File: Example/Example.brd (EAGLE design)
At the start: 86 x 54 mm, 14 parts, among them IC1 LM555D, J1 UX60-MB-5S8, Q1 SSM3J356R, Q2 BSS806N, SW1 MFS101D-6-Z

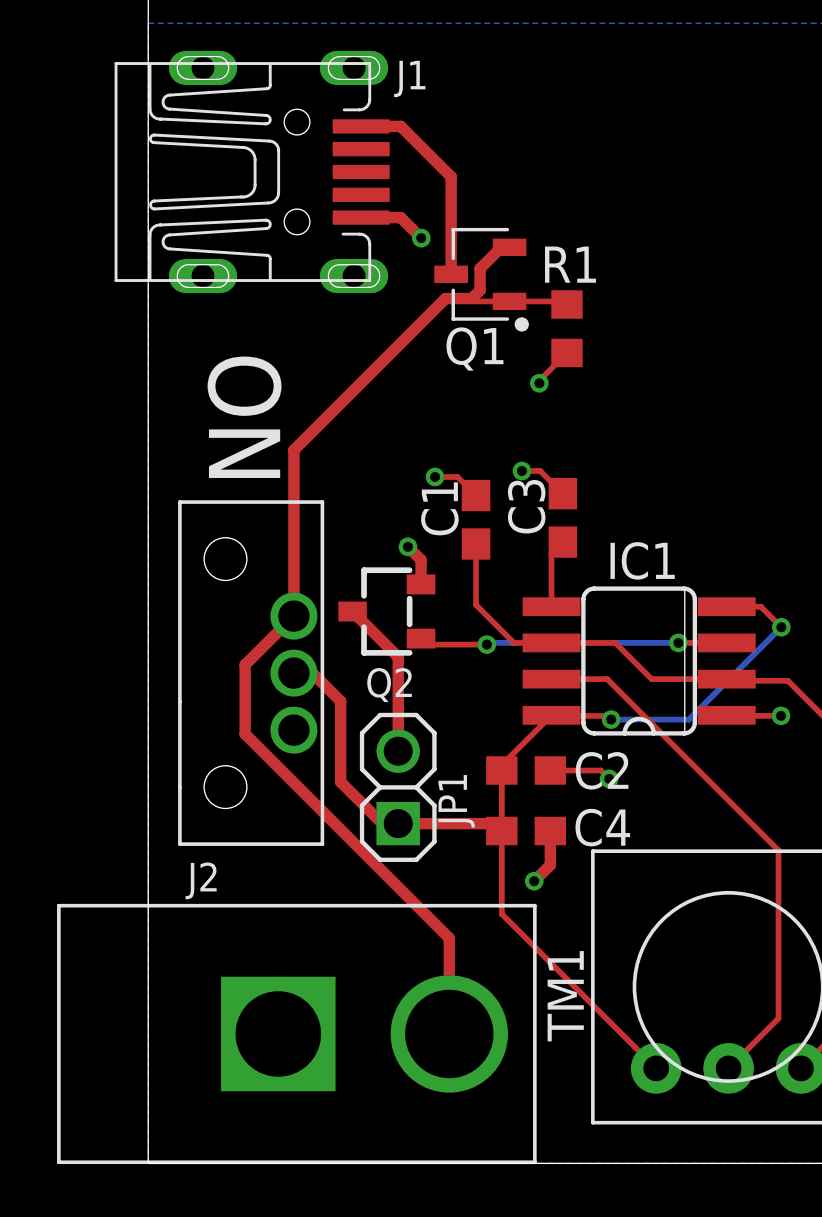
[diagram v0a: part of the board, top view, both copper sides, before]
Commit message: Fixed broken circuit and made new render
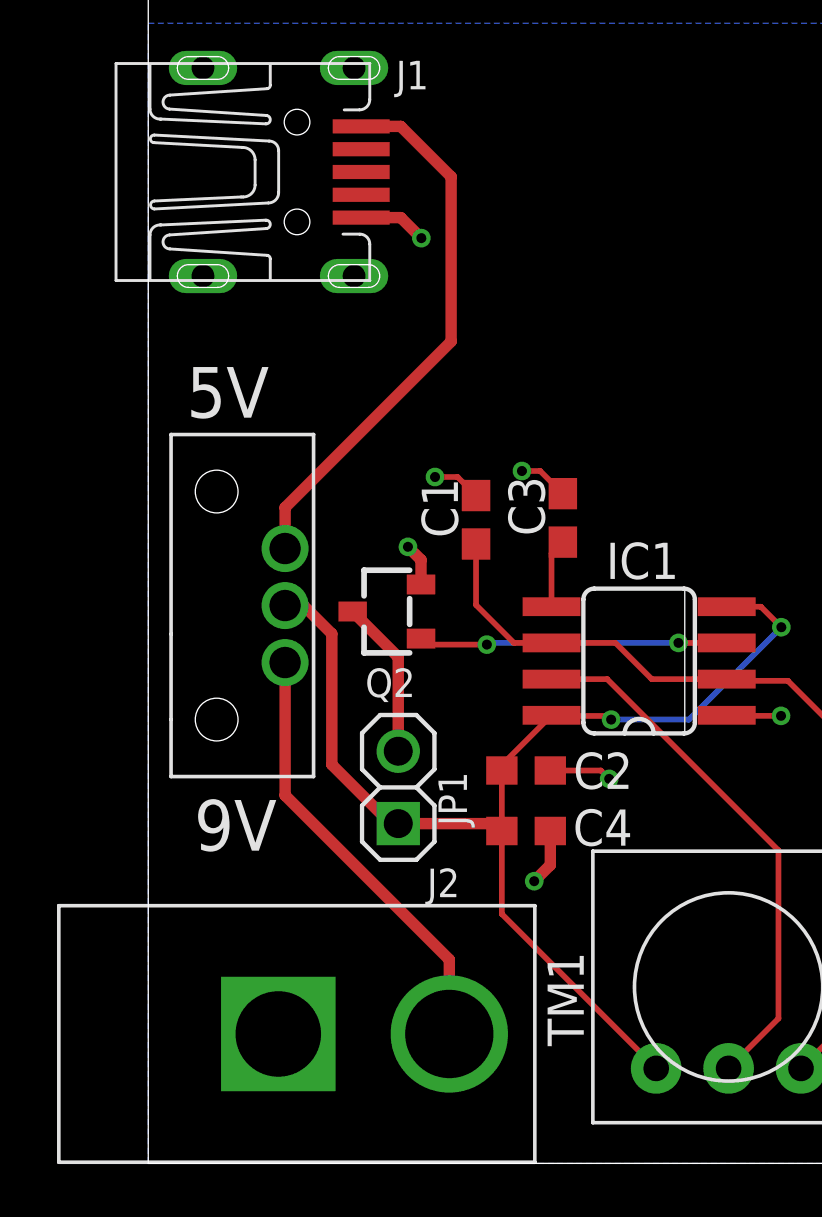
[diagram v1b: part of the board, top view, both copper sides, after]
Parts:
- removed Q1: SSM3J356R, Example:SOT95P240X80-3N
- removed R1: 10K, rcl:R0603
- moved SW1 2.39 mm to (4.80, 19.6)
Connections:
- net GND: no longer R1.1
- net N$4: now also SW1.3; no longer Q1.3
- net N$6: now also SW1.1; no longer Q1.1, Q1.2, R1.2, SW1.3
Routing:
- net N$6: track 38.5 -> 15.4 mm
- net N$4: track 7.31 -> 19.3 mm
- net +9V: track 38.3 -> 40.6 mm
- net GND: track 14.9 -> 13.5 mm, vias 8 -> 7
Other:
- board text added: "5V"
- board text added: "9V"
- board text removed: "ON"
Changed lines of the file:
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@@
 <?xml version="1.0" encoding="utf-8"?>
 <!DOCTYPE eagle SYSTEM "eagle.dtd">
-<eagle version="9.6.2">
+<eagle version="9.5.2">
 <drawing>
 <settings>
-<setting alwaysvectorfont="no"/>
+<setting alwaysvectorfont="yes"/>
 <setting verticaltext="up"/>
 </settings>
-<grid distance="50" unitdist="mil" unit="mil" style="lines" multiple="1" display="no" altdistance="5" altunitdist="mil" altunit="mil"/>
+<grid distance="0.01" unitdist="mm" unit="mm" style="lines" multiple="1" display="no" altdistance="5" altunitdist="mil" altunit="mil"/>
 <layers>
 <layer number="1" name="Top" color="4" fill="1" visible="yes" active="yes"/>
@@
 </layers>
 <board>
-<fusionsync huburn="a.cGVyc29uYWw6dWUyY2EyMWFk" projecturn="a.cGVyc29uYWw6dWUyY2EyMWFkIzIwMjAxMTI1MzU2ODEzNTgx" f3durn="urn:adsk.wipprod:dm.lineage:dyqZrbbKTy2XcHXfwjEQZg" pcbguid="" lastpulledtime="" lastsyncedchangeguid="" latestrevisionid="17bb6422-26a5-4a22-a8fc-66dc1e53293f" lastsyncedrevisionid="17bb6422-26a5-4a22-a8fc-66dc1e53293f" lastboardhashguid="af3778a2-1b63-800d-478d-2496b3e21cb4" lastpushedtime="2020-11-26T02:07:45Z" linktopcb3d="false"/>
 <plain>
 <wire x1="0" y1="0" x2="86" y2="0" width="0" layer="20"/>
@@
 <wire x1="86" y1="54" x2="0" y2="54" width="0" layer="20"/>
 <wire x1="0" y1="54" x2="0" y2="0" width="0" layer="20"/>
-<text x="2.13" y="28.48" size="2.5" layer="21" font="vector" rot="SR270">ON</text>
 <text x="30.58" y="2.23" size="1.778" layer="21" font="vector" rot="R90">RoboJackets PCB Contest
 555 Timer PWM Motor Driver</text>
 <dimension x1="0" y1="54" x2="0" y2="0" x3="-13.1" y3="27" textsize="1.778" layer="51" dtype="vertical"/>
 <dimension x1="0" y1="54" x2="86" y2="54" x3="43" y3="63.84" textsize="1.778" layer="51" dtype="horizontal"/>
+<text x="1.34" y="26.16" size="1.778" layer="21">5V</text>
+<text x="1.61" y="10.97" size="1.778" layer="21">9V</text>
 </plain>
 <attributes>
@@
 </element>
 <element name="TM1" library="adafruit" library_urn="urn:adsk.eagle:library:420" package="TRIM-3386" package3d_urn="urn:adsk.eagle:package:6240934/1" value="" x="20.36" y="6.19" smashed="yes">
-<attribute name="NAME" x="15.28" y="4.285" size="1.27" layer="25" font="vector" rot="R90"/>
+<attribute name="NAME" x="15.28" y="4.115" size="1.27" layer="25" font="vector" rot="R90"/>
 <attribute name="VALUE" x="26.71" y="4.285" size="1.27" layer="27" rot="R90"/>
 </element>
 <element name="J2" library="RoboJackets-Connectors" package="PJ-037A" override_package3d_urn="urn:adsk.eagle:package:25000921/2" override_package_urn="urn:adsk.eagle:footprint:25000922/1" value="" x="4.562" y="4.54" smashed="yes">
 <attribute name="DKPN" value="CP-037A-ND" x="4.562" y="4.54" size="1.778" layer="27" display="off"/>
-<attribute name="NAME" x="1.372" y="9.54" size="1" layer="25" font="vector"/>
+<attribute name="NAME" x="9.782" y="9.34" size="1" layer="25" font="vector"/>
 <attribute name="VALUE" x="-2.438" y="-0.46" size="1" layer="27" font="vector" align="top-left"/>
 </element>
@@
 <attribute name="SPICEPREFIX" value="C" x="13.255" y="11.66" size="1.778" layer="27" display="off"/>
 </element>
-<element name="SW1" library="Example" package="MFS101D-6-Z" override_package3d_urn="urn:adsk.eagle:package:25000897/2" override_package_urn="urn:adsk.eagle:footprint:25000899/1" value="MFS101D-6-Z" x="5.11" y="17.2" smashed="yes" rot="R90">
-<attribute name="DKPN" value="563-1555-ND" x="5.11" y="17.2" size="1.778" layer="27" rot="R90" display="off"/>
-</element>
-<element name="R1" library="rcl" library_urn="urn:adsk.eagle:library:334" package="R0603" package3d_urn="urn:adsk.eagle:package:23555/3" value="10K" x="14.69" y="29.28" smashed="yes" rot="R90">
-<attribute name="NAME" x="13.765" y="30.895" size="1.27" layer="25" font="vector"/>
-<attribute name="POPULARITY" value="77" x="14.69" y="29.28" size="1.778" layer="27" rot="R90" display="off"/>
-<attribute name="SPICEPREFIX" value="R" x="14.69" y="29.28" size="1.778" layer="27" rot="R90" display="off"/>
-</element>
-<element name="Q1" library="Example" package="SOT95P240X80-3N" package3d_urn="urn:adsk.eagle:package:24993154/1" value="SSM3J356R" x="11.65" y="31.19" smashed="yes" rot="R180">
-<attribute name="NAME" x="11.49" y="29.3064" size="1.27" layer="25" font="vector" rot="R180" align="bottom-center"/>
+<element name="SW1" library="Example" package="MFS101D-6-Z" override_package3d_urn="urn:adsk.eagle:package:25000897/2" override_package_urn="urn:adsk.eagle:footprint:25000899/1" value="MFS101D-6-Z" x="4.8" y="19.57" smashed="yes" rot="R90">
+<attribute name="DKPN" value="563-1555-ND" x="4.8" y="19.57" size="1.778" layer="27" rot="R90" display="off"/>
 </element>
 </elements>
@@
 <wire x1="15.877" y1="13.783" x2="16.17" y2="13.49" width="0.2" layer="1"/>
 <via x="16.17" y="13.49" extent="1-16" drill="0.35"/>
-<contactref element="R1" pad="1"/>
-<wire x1="14.69" y1="28.43" x2="13.72" y2="27.46" width="0.2" layer="1"/>
-<wire x1="13.72" y1="27.46" x2="13.72" y2="27.37" width="0.2" layer="1"/>
-<via x="13.72" y="27.37" extent="1-16" drill="0.35"/>
 </signal>
 <signal name="+9V">
@@
 <contactref element="C4" pad="1"/>
 <contactref element="SW1" pad="2"/>
-<wire x1="6.75" y1="16.21" x2="5.76" y2="17.2" width="0.4" layer="1"/>
-<wire x1="5.11" y1="17.2" x2="5.76" y2="17.2" width="0.4" layer="1"/>
-<wire x1="6.75" y1="16.21" x2="6.75" y2="13.38" width="0.4" layer="1"/>
-<wire x1="6.75" y1="13.38" x2="8.21" y2="11.92" width="0.4" layer="1"/>
-<wire x1="8.21" y1="11.92" x2="8.77" y2="11.92" width="0.4" layer="1"/>
+<wire x1="6.44" y1="18.58" x2="5.45" y2="19.57" width="0.4" layer="1"/>
+<wire x1="4.8" y1="19.57" x2="5.45" y2="19.57" width="0.4" layer="1"/>
+<wire x1="6.44" y1="18.58" x2="6.44" y2="13.99" width="0.4" layer="1"/>
+<wire x1="8.77" y1="11.92" x2="8.51" y2="11.92" width="0.4" layer="1"/>
+<wire x1="8.51" y1="11.92" x2="6.44" y2="13.99" width="0.4" layer="1"/>
 <wire x1="14.1476" y1="15.719" x2="12.405" y2="13.9764" width="0.2" layer="1"/>
 <wire x1="12.405" y1="13.9764" x2="12.405" y2="13.783" width="0.4" layer="1"/>
@@
 <signal name="N$4">
 <contactref element="J1" pad="1"/>
-<contactref element="Q1" pad="3"/>
 <wire x1="7.47" y1="36.38" x2="8.86" y2="36.38" width="0.4" layer="1"/>
-<wire x1="10.6255" y1="34.6145" x2="10.6255" y2="31.19" width="0.4" layer="1"/>
 <wire x1="8.86" y1="36.38" x2="10.6255" y2="34.6145" width="0.4" layer="1"/>
+<contactref element="SW1" pad="3"/>
+<wire x1="10.6255" y1="34.6145" x2="10.6255" y2="28.8355" width="0.4" layer="1"/>
+<wire x1="4.8" y1="23.01" x2="4.8" y2="21.57" width="0.4" layer="1"/>
+<wire x1="10.6255" y1="28.8355" x2="4.8" y2="23.01" width="0.4" layer="1"/>
 </signal>
 <signal name="N$6">
-<contactref element="R1" pad="2"/>
-<contactref element="Q1" pad="1"/>
-<wire x1="14.58" y1="30.24" x2="12.6745" y2="30.24" width="0.2" layer="1"/>
-<wire x1="14.58" y1="30.24" x2="14.69" y2="30.13" width="0.2" layer="1"/>
 <contactref element="J2" pad="P$2"/>
-<contactref element="SW1" pad="3"/>
-<contactref element="Q1" pad="2"/>
-<wire x1="10.562" y1="7.898" x2="10.562" y2="4.54" width="0.4" layer="1"/>
-<wire x1="3.4" y1="15.06" x2="3.4" y2="17.49" width="0.4" layer="1"/>
-<wire x1="10.562" y1="7.898" x2="3.4" y2="15.06" width="0.4" layer="1"/>
-<wire x1="5.11" y1="19.2" x2="3.4" y2="17.49" width="0.4" layer="1"/>
-<wire x1="5.11" y1="19.2" x2="5.11" y2="25.02" width="0.4" layer="1"/>
-<wire x1="10.43" y1="30.34" x2="11.35" y2="30.34" width="0.4" layer="1"/>
-<wire x1="11.35" y1="30.34" x2="11.64" y2="30.63" width="0.4" layer="1"/>
-<wire x1="11.64" y1="30.63" x2="11.64" y2="31.39" width="0.4" layer="1"/>
-<wire x1="11.64" y1="31.39" x2="12.39" y2="32.14" width="0.4" layer="1"/>
-<wire x1="12.39" y1="32.14" x2="12.6745" y2="32.14" width="0.4" layer="1"/>
-<wire x1="5.11" y1="25.02" x2="10.43" y2="30.34" width="0.4" layer="1"/>
-<wire x1="12.6745" y1="30.24" x2="11.45" y2="30.24" width="0.2" layer="1"/>
-<wire x1="11.45" y1="30.24" x2="11.35" y2="30.34" width="0.2" layer="1"/>
+<wire x1="10.562" y1="7.148" x2="10.562" y2="4.54" width="0.4" layer="1"/>
+<wire x1="10.562" y1="7.148" x2="4.8" y2="12.91" width="0.4" layer="1"/>
+<wire x1="4.8" y1="12.91" x2="4.8" y2="17.57" width="0.4" layer="1"/>
+<contactref element="SW1" pad="1"/>
 </signal>
 </signals>
@@
 </note>
 <note version="8.3" severity="warning">
-Since Version 8.3, EAGLE supports Fusion synchronisation.
-This feature will not be available in this version and saving
-the document will break the link to the Fusion PCB feature.
-</note>
-<note version="8.3" severity="warning">
